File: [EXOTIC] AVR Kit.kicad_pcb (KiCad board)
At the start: 2 copper layers, 124.5 x 71.1 mm, 54 parts, among them J1 Barrel_Jack_Switch, J2 AVR-ISP-10, J3 USB_B, J4 Conn_01x08_Socket, J5 Conn_01x08_Socket, J6 Conn_01x09_Socket, J7 Conn_01x07_Socket, Q1 AO3401A, Q2 SI2302, SW1 SW_Push, SW2 SW_DPDT_x2, U1 ATmega32A-P, U2 AMS1117-5.0, U3 AMS1117-3.3, U4 LM324, U5 LM339, U6 CH340C, Y1 16 MHz

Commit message: Rev 2.1
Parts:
- moved J6 20.9 mm to (149.2, 138.4), turned to 90 degrees
- moved J4 2.74 mm to (200.7, 138.4)
- moved J7 1.37 mm to (159.4, 105.4)
- moved C1 1.37 mm to (164.3, 102.2)
- moved C2 1.37 mm to (172.3, 102.2)
- moved J5 1.37 mm to (197.5, 105.4)
- moved Y1 0.82 mm to (168.3, 106.7)
- moved J1 0.63 mm to (99.7, 102.9)
- moved L1 0.63 mm to (174.6, 139.7)
- moved C3 0.52 mm to (179.1, 137.8)
- moved C4 0.52 mm to (174.6, 135.9)
- moved U1 0.52 mm to (173.4, 121.9)
- moved J3 0.41 mm to (101.0, 139.0)
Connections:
- J6 pad 1: /PC7 -> /PD7
- J6 pad 2: /PC6 -> /PC0
- J6 pad 3: /TDI -> /PC1
- J6 pad 4: /TDO -> /TCK
- J6 pad 6: /TCK -> /TDO
- J6 pad 7: /PC1 -> /TDI
- J6 pad 8: /PC0 -> /PC6
- J6 pad 9: /PD7 -> /PC7
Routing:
- net /~{RESET}: track 260.6 -> 252.3 mm
- net GND: track 14.6 -> 7.57 mm
- net unconnected-(J3-Shield-Pad5): track 12.0 -> 15.0 mm
- net /PA7: track 12.3 -> 10.2 mm
- net /PA6: track 12.3 -> 10.2 mm
- net /PA3: track 12.3 -> 10.2 mm
- net /PA0: track 12.3 -> 10.2 mm
- net /PA4: track 12.3 -> 10.2 mm
- net /PA5: track 12.3 -> 10.2 mm
- net /PA2: track 12.3 -> 10.2 mm
- net /PA1: track 12.3 -> 10.2 mm
- net VBUS: track 60.7 -> 62.4 mm
- net /SCK: track 60.2 -> 58.7 mm
- net /MISO: track 60.9 -> 59.4 mm
- net +5V: track 260.2 -> 258.9 mm
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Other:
- board text added: "A0"
- board text added: "A1"
- board text added: "A2"
- board text added: "A3"
- board text added: "A4"
- board text added: "A5"
- board text added: "A6"
- board text added: "A7"
- board text added: "B0"
- board text added: "B1"
- board text added: "B2"
- board text added: "B3"
- board text added: "B4"
- board text added: "B5"
- board text added: "B6"
- board text added: "B7"
- board text added: "C0"
- board text added: "C1"
- board text added: "C2"
- board text added: "C3"
- board text added: "C4"
- board text added: "C5"
- board text added: "C6"
- board text added: "C7"
- board text added: "D0"
- board text added: "D1"
- board text added: "D2"
- board text added: "D3"
- board text added: "D4"
- board text added: "D5"
- board text added: "D6"
- board text added: "D7"
- board text added: "Developed & Designed By Morad Tamer Revision ${REVISION} ${ISSUE_DATE}"
- board text added: "MISO"
- board text added: "MOSI"
- board text added: "PORT A"
- board text added: "PORT B"
- board text added: "PORT C"
- board text added: "PORT D"
- board text added: "RX"
- board text added: "SCK"
- board text added: "TCK"
- board text added: "TDI"
- board text added: "TDO"
- board text added: "TMS"
- board text added: "TX"
- board text added: "~{SS}"
- board text removed: "Developed & Designed By Morad Tamer Revisiom ${REVISION} ${ISSUE_DATE}"

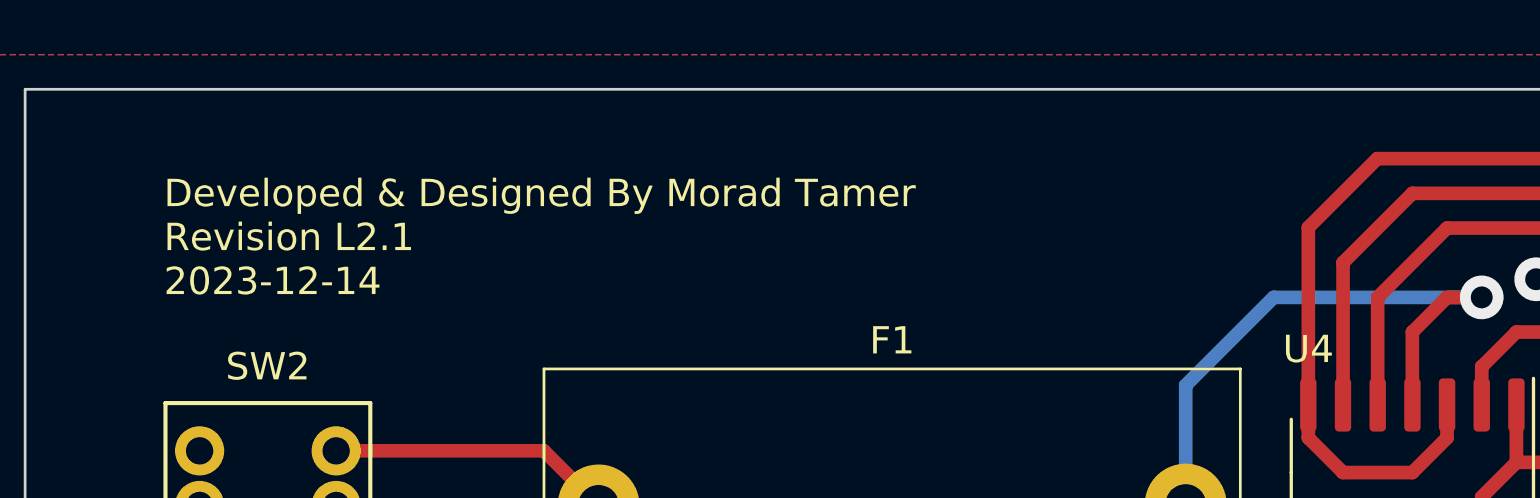
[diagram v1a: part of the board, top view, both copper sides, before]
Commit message: Update [EXOTIC] AVR Kit.kicad_pcb
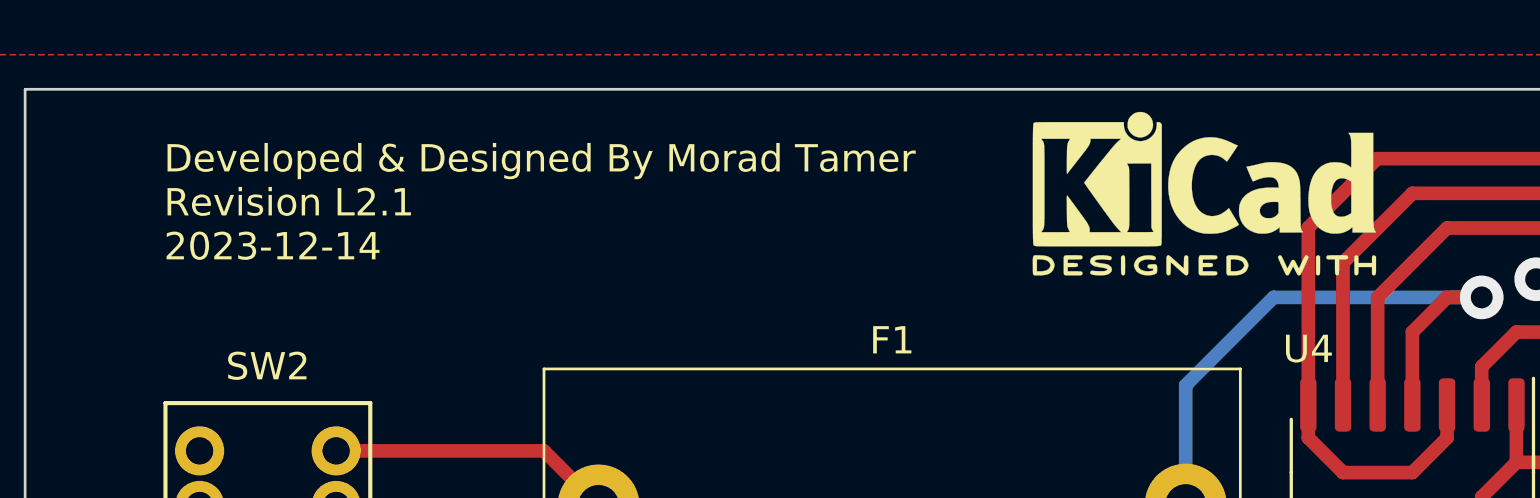
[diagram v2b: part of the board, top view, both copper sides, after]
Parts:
- added REF**: KiCad-Logo2_5mm_SilkScreen, Symbol:KiCad-Logo2_5mm_SilkScreen, F.Cu at (128.3, 80.0)

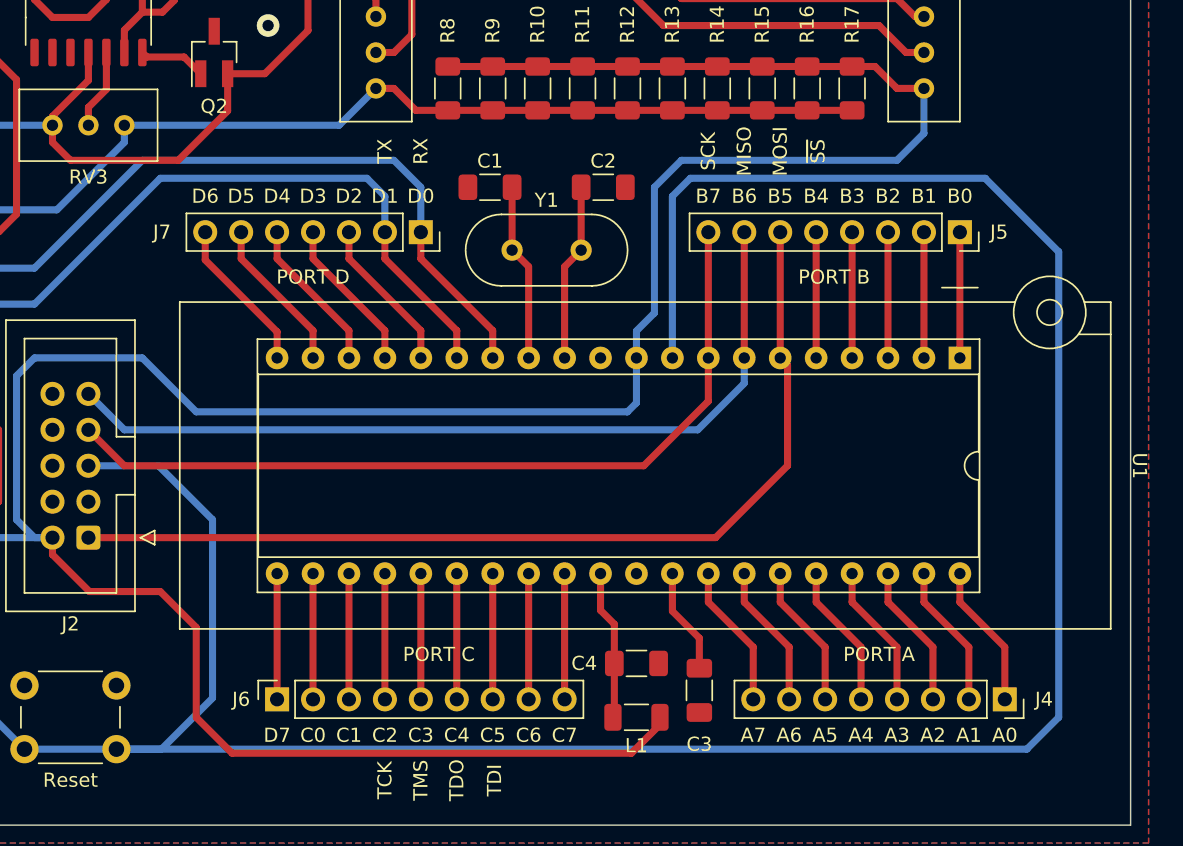
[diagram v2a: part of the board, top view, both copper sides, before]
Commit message: Update [EXOTIC] AVR Kit.kicad_pcb
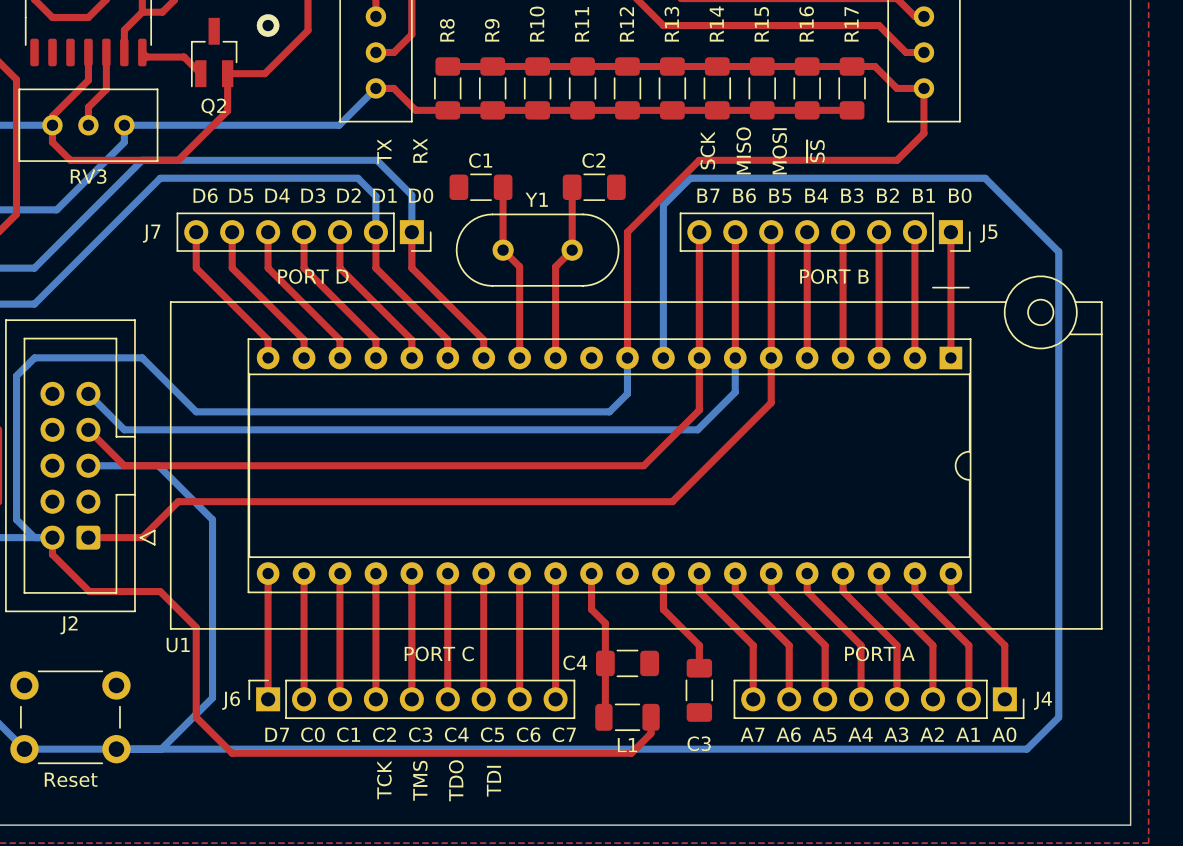
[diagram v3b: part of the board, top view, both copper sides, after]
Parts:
- moved C1 0.64 mm to (163.6, 102.2)
- moved J5 0.64 mm to (196.8, 105.4)
- moved Y1 0.64 mm to (167.6, 106.7)
- moved C2 0.63 mm to (171.6, 102.2)
- moved C4 0.63 mm to (174.0, 135.9)
- moved J6 0.63 mm to (148.6, 138.4)
- moved J7 0.63 mm to (158.8, 105.4)
- moved L1 0.63 mm to (174.0, 139.7)
- moved U1 0.63 mm to (172.7, 121.9)
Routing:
- net /MOSI: track 68.2 -> 64.3 mm
- net +5V: track 258.9 -> 257.1 mm
- net /RX <--: track 85.9 -> 84.9 mm
- net /TX -->: track 90.0 -> 89.3 mm

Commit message: WIP
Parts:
- removed R10, R11, R12, R13, R14, R15, R16, R17: 1 Ω, Resistor_SMD:R_1206_3216Metric_Pad1.30x1.75mm_HandSolder
- added G***: LOGO, M's Library:TeamExotic_Logo_H40mm, B.Cu at (-17.8, 85.1)
- added J8: ICSP_Connector, Connector_PinHeader_2.54mm:PinHeader_2x03_P2.54mm_Vertical, F.Cu at (234.9, 133.3)
- added REF**: Polarity_Center_Positive_6mm_SilkScreen, Symbol:Polarity_Center_Positive_6mm_SilkScreen, B.Cu at (-88.3, 113.0)
- R8, R9: footprint Resistor_SMD:R_1206_3216Metric_Pad1.30x1.75mm_HandSolder -> Resistor_THT:R_Axial_DIN0614_L14.3mm_D5.7mm_P7.62mm_Vertical
- moved REF** 191.9 mm to (-63.5, 73.7)
- moved G*** 191.9 mm to (-72.4, 128.3)
- moved R4 71.1 mm to (59.7, 141.0)
- moved R5 69.9 mm to (59.7, 147.3), turned to 90 degrees
- moved C9 67.1 mm to (82.5, 176.5), turned to -90 degrees
- moved R6 66.7 mm to (53.3, 135.9)
- moved U5 66.7 mm to (53.3, 143.5)
- moved Q1 58.0 mm to (52.4, 151.1)
- moved SW1 54.8 mm to (97.2, 178.8)
- moved RV2 43.0 mm to (152.4, 96.5), turned to -90 degrees
- moved R1 36.2 mm to (129.5, 139.4)
- moved RV3 31.9 mm to (165.1, 95.2), turned to 0 degrees
- moved U3 27.7 mm to (138.4, 99.1), turned to 180 degrees
- moved R9 27.6 mm to (137.2, 91.4)
- moved U4 27.4 mm to (163.2, 87.6), turned to 0 degrees
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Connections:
- R9 pad 1: +5V_{OCP} -> +5V
- R9 pad 2: +5V -> +5V_{OCP}
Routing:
- net /~{RESET}: track 252.6 -> 8.48 mm, vias 1 -> 0
- net +5V: track 257.1 -> 55.0 mm, vias 1 -> 0
- net Net-(U4A-+): track 83.7 -> 18.4 mm
- net Net-(U4B--): track 73.1 -> 9.90 mm
- net VBUS: track 62.4 -> 0.00 mm, vias 1 -> 0
- net /MISO: track 59.2 -> 95.3 mm
- net +5V_{OCP}: track 86.2 -> 50.2 mm, vias 1 -> 0
- net Net-(U4B-+): track 40.9 -> 10.4 mm
- net Net-(Q1-G): track 43.9 -> 15.7 mm
- net /SCK: track 58.4 -> 85.6 mm
- net /TX -->: track 89.3 -> 71.9 mm
- net +3V3: track 29.4 -> 12.6 mm
- net /USB_D+: track 16.2 -> 0.00 mm
- net /USB_D-: track 16.2 -> 0.00 mm
- net unconnected-(J3-Shield-Pad5): track 15.0 -> 0.00 mm
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- removed copper zone on B.Cu, net GND
- removed copper zone on F.Cu, net GND
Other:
- board outline removed
- board text added: "PORT D7"
- board text removed: "D7"

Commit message: Rev. 3
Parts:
- moved J1 16.3 mm to (116.3, 95.2), turned to 90 degrees
- moved SW2 11.6 mm to (104.1, 91.4), turned to 0 degrees
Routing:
- net Net-(SW2B-B): track 0.00 -> 3.83 mm
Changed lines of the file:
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@@
   )
   (footprint "M's Library:BarrelJack_Horizontal" (layer "F.Cu")
-    (at 100.13 96.52 180)
+    (at 116.332 95.25 90)
     (descr "DC Barrel Jack")
     (tags "Power Jack")
@@
     (property "ki_keywords" "DC power barrel jack connector")
     (attr through_hole)
-    (fp_text reference "J1" (at 6.985 -5.715) (layer "F.SilkS")
+    (fp_text reference "J1" (at 6.985 -5.715 90) (layer "F.SilkS")
         (effects (font (size 1 1) (thickness 0.15)))
     )
-    (fp_text value "Barrel_Jack_Switch" (at 6.35 -5.715) (layer "F.Fab")
+    (fp_text value "Barrel_Jack_Switch" (at 6.35 -5.715 90) (layer "F.Fab")
         (effects (font (size 1 1) (thickness 0.15)))
     )
-    (fp_text user "${REFERENCE}" (at 6.35 -7.62) (layer "F.Fab")
+    (fp_text user "${REFERENCE}" (at 6.35 -7.62 90) (layer "F.Fab")
         (effects (font (size 1 1) (thickness 0.15)))
     )
@@
     (fp_line (start 13.55 4.5) (end 13.55 -4.5)
       (stroke (width 0.1) (type default)) (layer "F.Fab"))
-    (pad "1" thru_hole rect (at 0 0 180) (size 2.5 5) (drill oval 1 3.5) (layers "*.Cu" "*.Mask")
+    (pad "1" thru_hole rect (at 0 0 90) (size 2.5 5) (drill oval 1 3.5) (layers "*.Cu" "*.Mask")
       (net 87 "Net-(SW2B-B)") (pintype "passive"))
-    (pad "2" thru_hole oval (at 2.85 -5 180) (size 5 2.5) (drill oval 3.5 1) (layers "*.Cu" "*.Mask")
+    (pad "2" thru_hole oval (at 2.85 -5 90) (size 5 2.5) (drill oval 3.5 1) (layers "*.Cu" "*.Mask")
       (net 7 "-V_{In}") (pintype "passive"))
-    (pad "3" thru_hole oval (at 6.15 0 180) (size 2.5 5) (drill oval 1 3.5) (layers "*.Cu" "*.Mask")
+    (pad "3" thru_hole oval (at 6.15 0 90) (size 2.5 5) (drill oval 1 3.5) (layers "*.Cu" "*.Mask")
       (net 16 "unconnected-(J1-Pad3)") (pintype "passive+no_connect"))
     (model "${KIPRJMOD}/packages3D/BarrelJack_Horizontal.wrl"
@@
   )
   (footprint "M's Library:SW_Push_DPDT_Toggle_7.0mm" (layer "F.Cu")
-    (at 94.415 85.09 90)
+    (at 104.14 91.44)
     (descr "momentary / push-push button, h=17.5mm C&K PVA2 https://www.ckswitches.com/media/1343/pva.pdf")
     (tags "tact sw push PVA2 DPDT")
@@
     (property "ki_keywords" "switch dual-pole double-throw DPDT spdt ON-ON")
     (attr through_hole)
-    (fp_text reference "SW2" (at 5.08 0 180) (layer "F.SilkS")
+    (fp_text reference "SW2" (at 5.08 0 90) (layer "F.SilkS")
         (effects (font (size 1 1) (thickness 0.15)))
     )
-    (fp_text value "SW_DPDT_x2" (at 0 6 90) (layer "F.Fab")
+    (fp_text value "SW_DPDT_x2" (at 0 6) (layer "F.Fab")
         (effects (font (size 1 1) (thickness 0.15)))
     )
-    (fp_text user "${REFERENCE}" (at 0 0 90) (layer "F.Fab")
+    (fp_text user "${REFERENCE}" (at 0 0) (layer "F.Fab")
         (effects (font (size 1 1) (thickness 0.15)))
     )
@@
     (fp_rect (start 2 -2) (end -2 2)
       (stroke (width 0.1) (type default)) (fill none) (layer "F.Fab"))
-    (pad "1" thru_hole rect (at -2 -2.5 90) (size 1.8 1.8) (drill 1) (layers "*.Cu" "*.Mask")
+    (pad "1" thru_hole rect (at -2 -2.5) (size 1.8 1.8) (drill 1) (layers "*.Cu" "*.Mask")
       (net 60 "unconnected-(SW2A-A-Pad1)") (pinfunction "A") (pintype "passive+no_connect"))
-    (pad "2" thru_hole circle (at 0 -2.5 90) (size 1.8 1.8) (drill 1) (layers "*.Cu" "*.Mask")
+    (pad "2" thru_hole circle (at 0 -2.5) (size 1.8 1.8) (drill 1) (layers "*.Cu" "*.Mask")
       (net 62 "unconnected-(SW2A-B-Pad2)") (pinfunction "B") (pintype "passive+no_connect"))
-    (pad "3" thru_hole circle (at 2 -2.5 90) (size 1.8 1.8) (drill 1) (layers "*.Cu" "*.Mask")
+    (pad "3" thru_hole circle (at 2 -2.5) (size 1.8 1.8) (drill 1) (layers "*.Cu" "*.Mask")
       (net 63 "unconnected-(SW2A-C-Pad3)") (pinfunction "C") (pintype "passive+no_connect"))
-    (pad "4" thru_hole circle (at -2 2.5 90) (size 1.8 1.8) (drill 1) (layers "*.Cu" "*.Mask")
+    (pad "4" thru_hole circle (at -2 2.5) (size 1.8 1.8) (drill 1) (layers "*.Cu" "*.Mask")
       (net 61 "unconnected-(SW2B-A-Pad4)") (pinfunction "A") (pintype "passive+no_connect"))
-    (pad "5" thru_hole circle (at 0 2.5 90) (size 1.8 1.8) (drill 1) (layers "*.Cu" "*.Mask")
+    (pad "5" thru_hole circle (at 0 2.5) (size 1.8 1.8) (drill 1) (layers "*.Cu" "*.Mask")
       (net 87 "Net-(SW2B-B)") (pinfunction "B") (pintype "passive"))
-    (pad "6" thru_hole circle (at 2 2.5 90) (size 1.8 1.8) (drill 1) (layers "*.Cu" "*.Mask")
+    (pad "6" thru_hole circle (at 2 2.5) (size 1.8 1.8) (drill 1) (layers "*.Cu" "*.Mask")
       (net 15 "Net-(SW2B-C)") (pinfunction "C") (pintype "passive"))
     (model "${KIPRJMOD}/packages3D/ON_ON_7x7mm_6pin.step"
@@
   (segment (start 59.41 146.05) (end 59.69 145.77) (width 0.4) (layer "F.Cu") (net 86))
   (segment (start 55.815 146.05) (end 59.41 146.05) (width 0.4) (layer "F.Cu") (net 86))
+  (segment (start 114.3 95.25) (end 113.03 96.52) (width 0.4) (layer "F.Cu") (net 87))
+  (segment (start 116.332 95.25) (end 114.3 95.25) (width 0.4) (layer "F.Cu") (net 87))
   (group "" (id 9b88c06d-eb93-41e5-bbf1-161242613859)
     (members

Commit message: Rev 3.1
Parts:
- removed J8: ICSP_Connector, Connector_PinHeader_2.54mm:PinHeader_2x03_P2.54mm_Vertical
- removed the R5 at (59.7, 147.3)
- removed REF**: KiCad-Logo2_5mm_SilkScreen, Symbol:KiCad-Logo2_5mm_SilkScreen
- removed REF**: Polarity_Center_Positive_6mm_SilkScreen, Symbol:Polarity_Center_Positive_6mm_SilkScreen
- added R11: 0 Ω, Resistor_SMD:R_1206_3216Metric_Pad1.30x1.75mm_HandSolder, F.Cu at (186.7, 109.2)
- added R9: 0 Ω, Resistor_SMD:R_1206_3216Metric_Pad1.30x1.75mm_HandSolder, F.Cu at (156.8, 97.8)
- D1: footprint LED_THT:LED_D5.0mm_Clear -> LED_SMD:LED_1206_3216Metric_Pad1.42x1.75mm_HandSolder
- moved G*** 293.4 mm to (219.7, 156.2)
- moved G*** 241.0 mm to (216.6, 141.3), turned to 90 degrees
- moved R4 111.8 mm to (156.8, 85.7), turned to 0 degrees
- moved C9 95.8 mm to (153.7, 112.4), turned to 0 degrees
- moved Q1 91.9 mm to (138.4, 118.7), turned to 0 degrees
- moved U5 90.6 mm to (137.2, 109.2)
- moved R5 87.1 mm to (138.1, 115.6)
- moved C10 60.8 mm to (153.7, 100.3), turned to 180 degrees
- moved J3 56.4 mm to (141.0, 99.3), turned to 90 degrees
- moved SW1 54.4 mm to (146.8, 156.2)
- moved C6 53.5 mm to (181.6, 97.9)
- moved C7 53.5 mm to (191.8, 108.0)
- moved C8 53.5 mm to (176.5, 91.5)
- moved F1 53.5 mm to (170.2, 106.7)
- moved R7 53.5 mm to (196.8, 88.9)
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- renumbered R6 to R5, R7 to R6, R8 to R7, R9 to R8
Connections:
- F1 pad 1: Net-(SW2B-C) -> Net-(SW2B-B)
- J1 pad 1: Net-(SW2B-B) -> Net-(SW2B-C)
- R4 pad 1: Net-(U5D-+) -> GND
- R4 pad 2: +V_{In} -> Net-(SW2B-C)
- U5 pad 14: Net-(Q1-G) -> unconnected-(U5-Pad14)
- U5 pad 2: unconnected-(U5-Pad2) -> Net-(Q1-G)
- U5 pad 4: unconnected-(U5A---Pad4) -> Net-(U5A--)
- U5 pad 5: unconnected-(U5A-+-Pad5) -> Net-(SW2B-C)
- U5 pad 8: +3V3 -> unconnected-(U5D---Pad8)
- U5 pad 9: Net-(U5D-+) -> unconnected-(U5D-+-Pad9)
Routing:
- net +5V: track 55.0 -> 284.1 mm, vias 0 -> 2
- net /~{RESET}: track 8.48 -> 228.6 mm
- net Net-(SW2B-C): track 0.00 -> 84.8 mm
- net /SCK: track 85.6 -> 169.7 mm
- net /RX <--: track 93.0 -> 32.4 mm, vias 1 -> 0
- net /MISO: track 95.3 -> 154.9 mm
- net Net-(U5A--): track 0.00 -> 46.5 mm
- net VBUS: track 0.00 -> 42.4 mm
- net /TX -->: track 71.9 -> 31.9 mm, vias 1 -> 0
- net Net-(R11-Pad2): track 0.00 -> 35.0 mm
- net /MOSI: track 54.2 -> 75.0 mm
- net Net-(Q2-G): track 3.41 -> 23.6 mm
- net unconnected-(J3-Shield-Pad5): track 0.00 -> 12.0 mm
- net /PD6: track 0.00 -> 11.0 mm
- net /PD5: track 0.00 -> 11.0 mm
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- added copper zone on B.Cu, net GND
- added copper zone on F.Cu, net GND
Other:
- board outline added: 104.1 x 80 mm
